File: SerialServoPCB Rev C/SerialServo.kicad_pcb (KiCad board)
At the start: 2 copper layers, 33.7 x 61.6 mm, 60 parts, among them J1 Conn_01x04, J2 Conn_01x05, J3 Conn_01x05, J4 Conn_01x03, J5 Conn_01x03, J6 Conn_01x03, J7 Conn_01x03, J8 Conn_01x02, SW1 SW_Push, SW2 SW_Push, SW3 SW_Push, U1 PIC16F1847-ISO, U2 LM358A

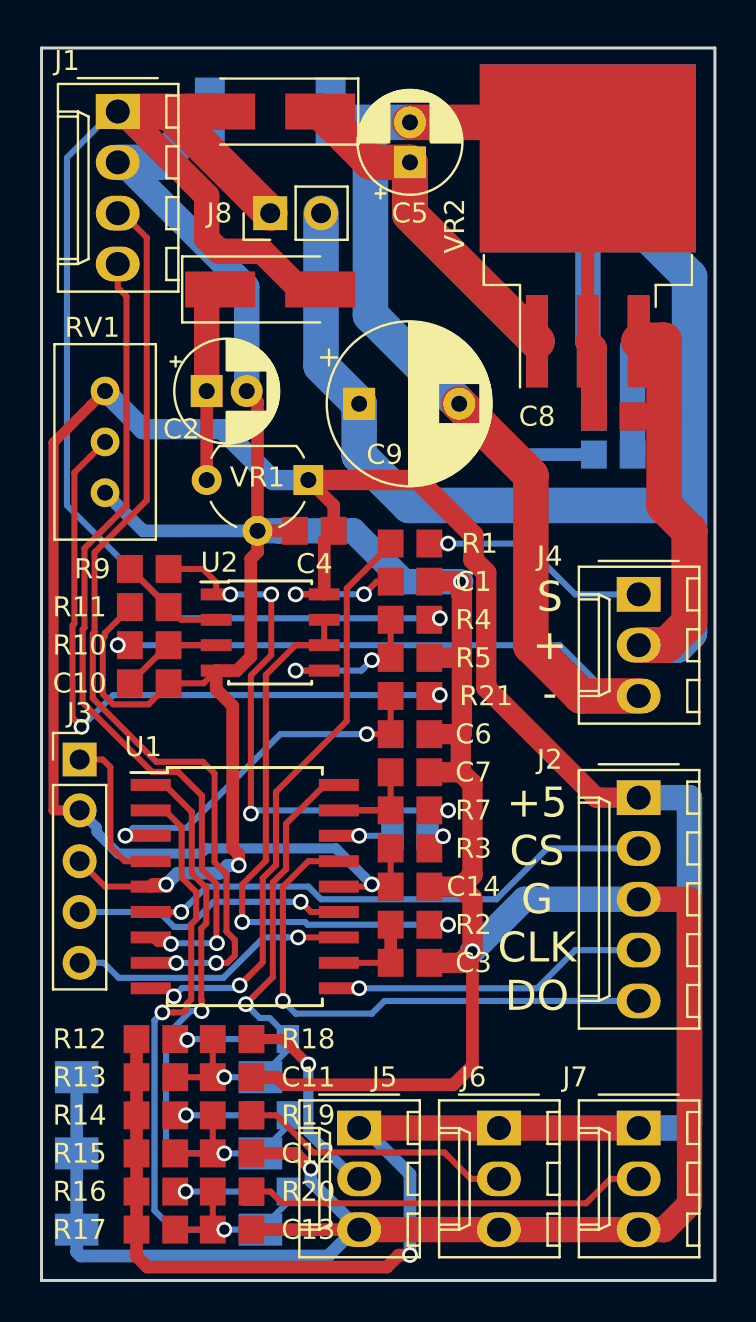
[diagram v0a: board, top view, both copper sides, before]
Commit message: ordered rev C
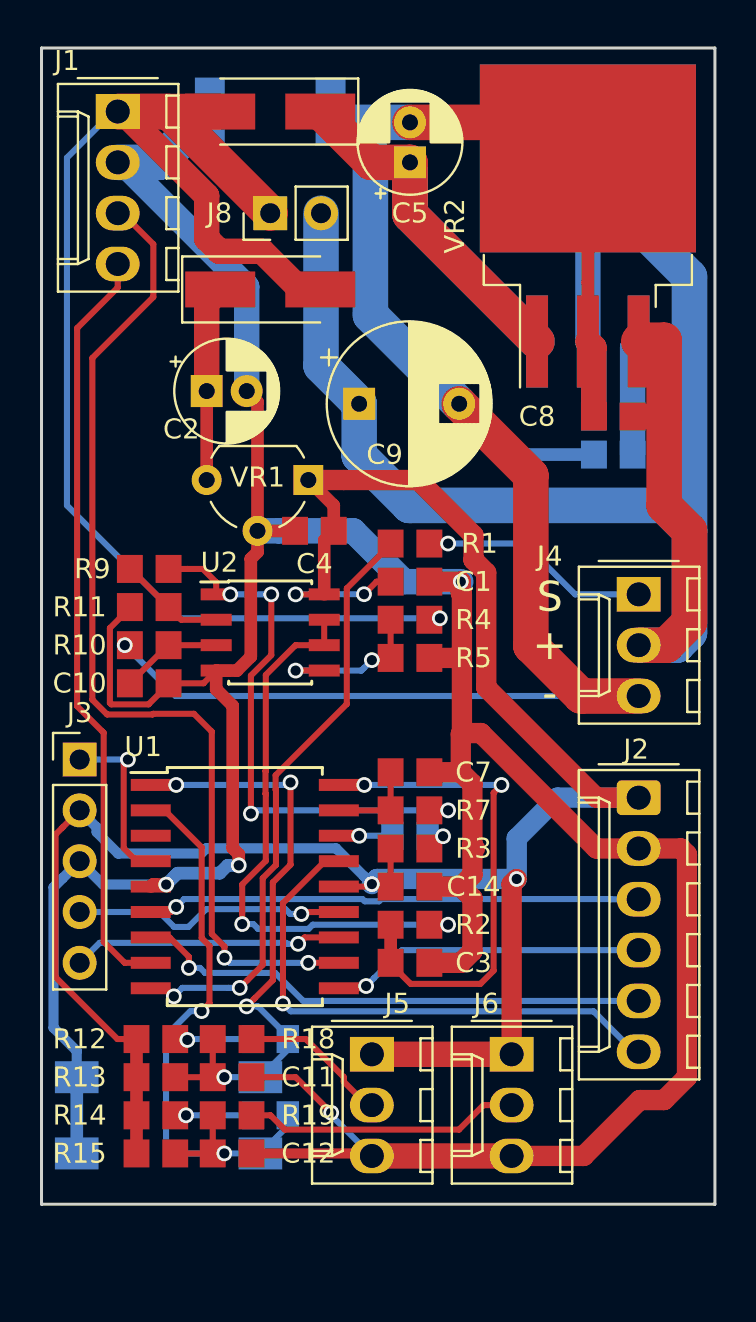
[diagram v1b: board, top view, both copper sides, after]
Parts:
- removed C13, C6: 0.1uF, Capacitor_SMD:C_0805_2012Metric_Pad1.29x1.40mm_HandSolder
- removed the D3 at (97.8, 136.5)
- removed J7: Conn_01x03, Connector_Molex:Molex_KK-254_AE-6410-03A_1x03_P2.54mm_Vertical
- removed R16, R20, R21: 1K0, Resistor_SMD:R_0805_2012Metric_Pad1.29x1.40mm_HandSolder
- removed R17: 47K, Resistor_SMD:R_0805_2012Metric_Pad1.29x1.40mm_HandSolder
- removed REF**: OSHW-Logo2_9.8x8mm_SilkScreen, Symbol:OSHW-Logo2_9.8x8mm_SilkScreen
- removed RV1: 20K, Potentiometer_THT:Potentiometer_Bourns_3296W_Vertical
- removed SW3: SW_Push, Button_Switch_SMD:SW_SPST_FSMSM
- J2: value Conn_01x05 -> Conn_01x06; footprint Connector_Molex:Molex_KK-254_AE-6410-05A_1x05_P2.54mm_Vertical -> Connector_Molex:Molex_KK-254_AE-6410-06A_1x06_P2.54mm_Vertical
- R6: value 1R0 -> 0R200 1W
- moved J5 3.74 mm to (102.9, 129.7)
- moved J6 3.74 mm to (109.9, 129.7)
- renumbered D4 to D3
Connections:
- J2 pad 2: ENC_CS -> GND
- J2 pad 3: GND -> ENC_CS
- J2 pad 5: Enc_DO -> MISO
- U1 pad 1: SW2_LED2 -> SW1_LED1
- U1 pad 11: Batt_V -> TX
- U1 pad 15: Enc_DO -> MOSI
- U1 pad 18: SW1_LED1 -> Batt_V
- U1 pad 2: SW3_LED3 -> SW2_LED2
- U1 pad 3: /AN4 -> Net-(U1-Pad3)
- U1 pad 7: RX -> MISO
- U1 pad 8: TX -> RX
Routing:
- net +5V: track 165.3 -> 114.1 mm
- net SW3_LED3: track 35.3 -> 0.00 mm, vias 2 -> 0
- net GND: track 214.9 -> 179.6 mm, vias 5 -> 4
- net Net-(R21-Pad1): track 34.2 -> 0.00 mm, vias 2 -> 0
- net MOSI: track 0.00 -> 27.5 mm, vias 0 -> 1
- net Enc_DO: track 27.3 -> 0.00 mm, vias 1 -> 0
- net MISO: track 0.00 -> 26.0 mm, vias 0 -> 1
- net Batt_V: track 4.49 -> 25.4 mm, vias 0 -> 2
- net Net-(J7-Pad2): track 20.1 -> 0.00 mm
- net /AN4: track 18.8 -> 0.00 mm, vias 2 -> 0
- net SW1_LED1: track 24.8 -> 30.6 mm, vias 2 -> 4
- net RX: track 42.0 -> 38.1 mm, vias 2 -> 0
- net Net-(D3-Pad2) (its old number): track 3.87 -> 0.00 mm, vias 1 -> 0
- net TX: track 47.6 -> 50.5 mm
- net Net-(J5-Pad2): track 10.3 -> 7.52 mm, vias 1 -> 0
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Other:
- board size 33.7 x 61.6 mm -> 33.7 x 57.8 mm
- rule pad_to_mask_clearance: 0.2 -> 0
- board text added: "+5 GND CS CLK MISO MOSI"
- board text added: "Serial Servo Rev C"
- board text removed: "+5 CS G CLK DO"
- board text removed: "Serial Servo Rev B"
